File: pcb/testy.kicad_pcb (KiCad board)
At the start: 2 copper layers, 114.5 x 101.4 mm, 102 parts, among them J1 L_B_LED, J2 R_B_LED, J3 SLAVE_LED, P1 OLED, P2 ICSP, SW0:0 SW_Push, SW0:1 SW_Push, SW0:2 SW_Push, SW0:3 SW_Push, SW0:4 SW_Push, SW1:0 SW_Push, SW1:1 SW_Push, SW1:2 SW_Push, SW1:3 SW_Push, SW1:4 SW_Push, SW2:0 SW_Push, SW2:1 SW_Push, SW2:2 SW_Push, SW2:3 SW_Push, SW2:4 SW_Push, SW3:0 SW_Push, SW3:1 SW_Push, SW3:2 SW_Push, SW3:3 SW_Push, SW3:4 SW_Push, SW3:5 SW_Push, SW4:1 SW_Push, SW4:2 SW_Push, SW4:3 SW_Push, SW4:4 SW_Push, SW4:5 SW_Push

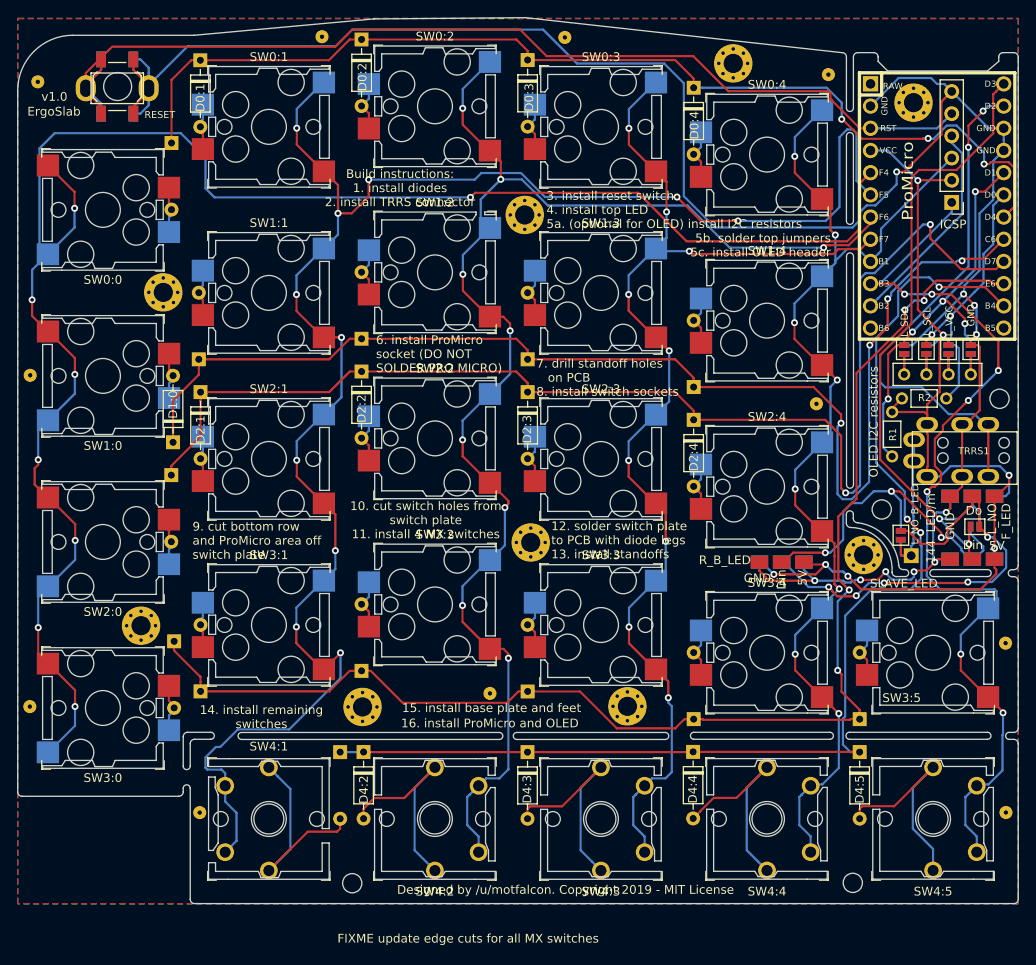
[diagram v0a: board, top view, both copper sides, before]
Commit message: fix: update edge cuts for MX switches, refresh PCB render
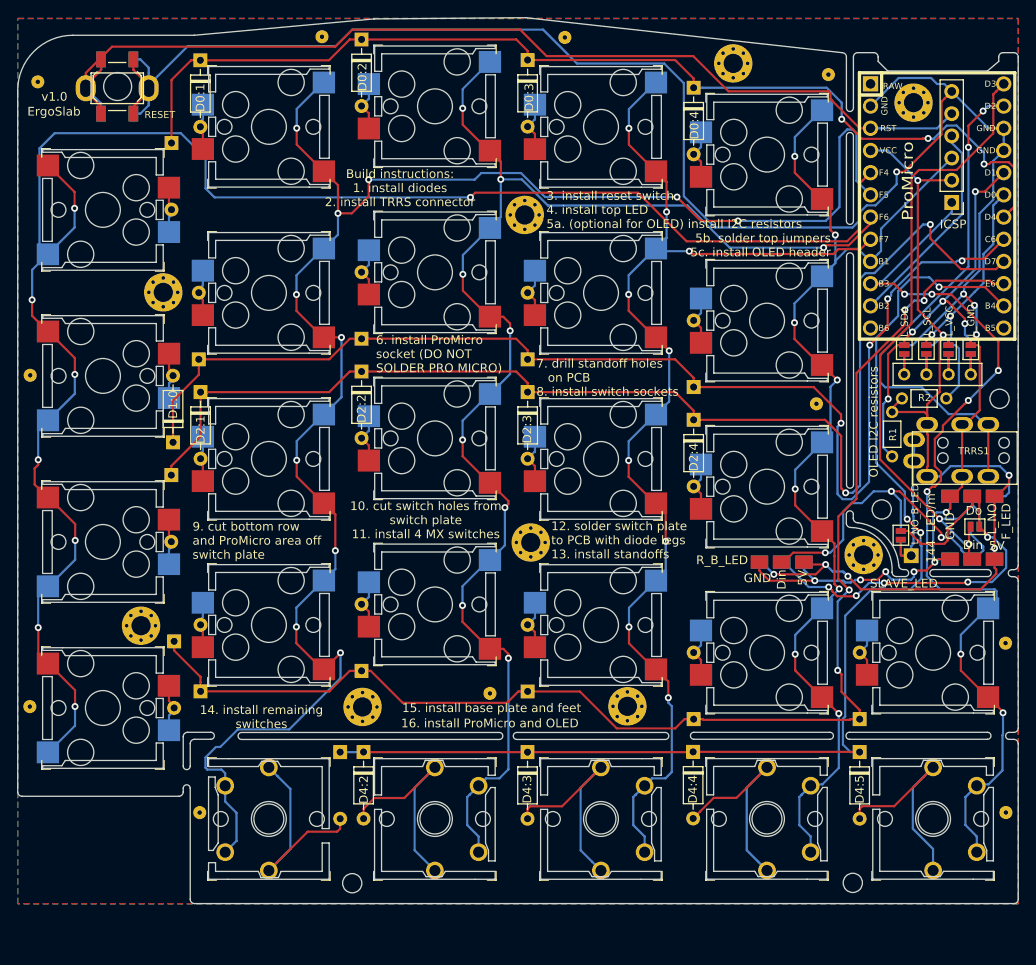
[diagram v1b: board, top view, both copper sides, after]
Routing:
- net Col2: track 160.7 -> 159.9 mm
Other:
- outline, holes or cut-outs redrawn
- board text added: "Designed by Tom Saleeba. Copyright 2019 - MIT License"
- board text removed: "Designed by /u/motfalcon. Copyright 2019 - MIT License"
- board text removed: "FIXME update edge cuts for all MX switches"
